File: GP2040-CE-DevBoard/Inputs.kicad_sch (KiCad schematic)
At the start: 21 parts

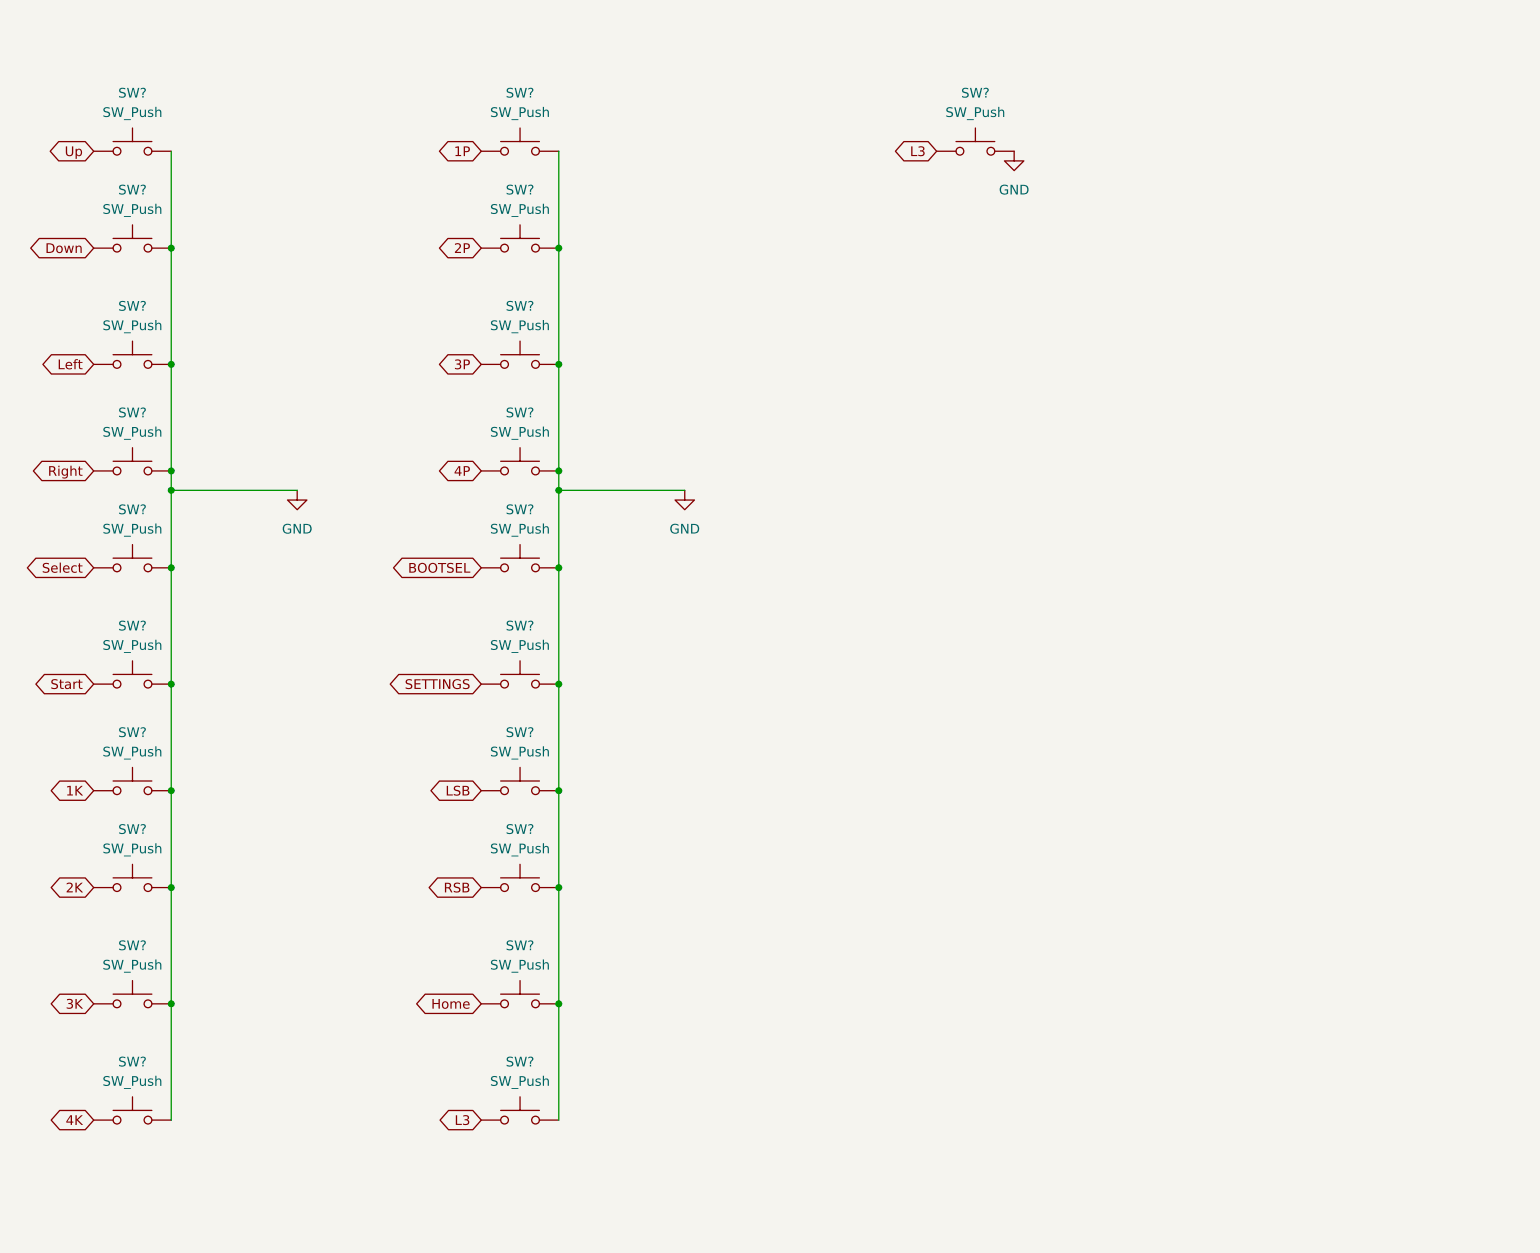
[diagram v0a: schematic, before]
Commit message: Schematic nearly complete, PCB started
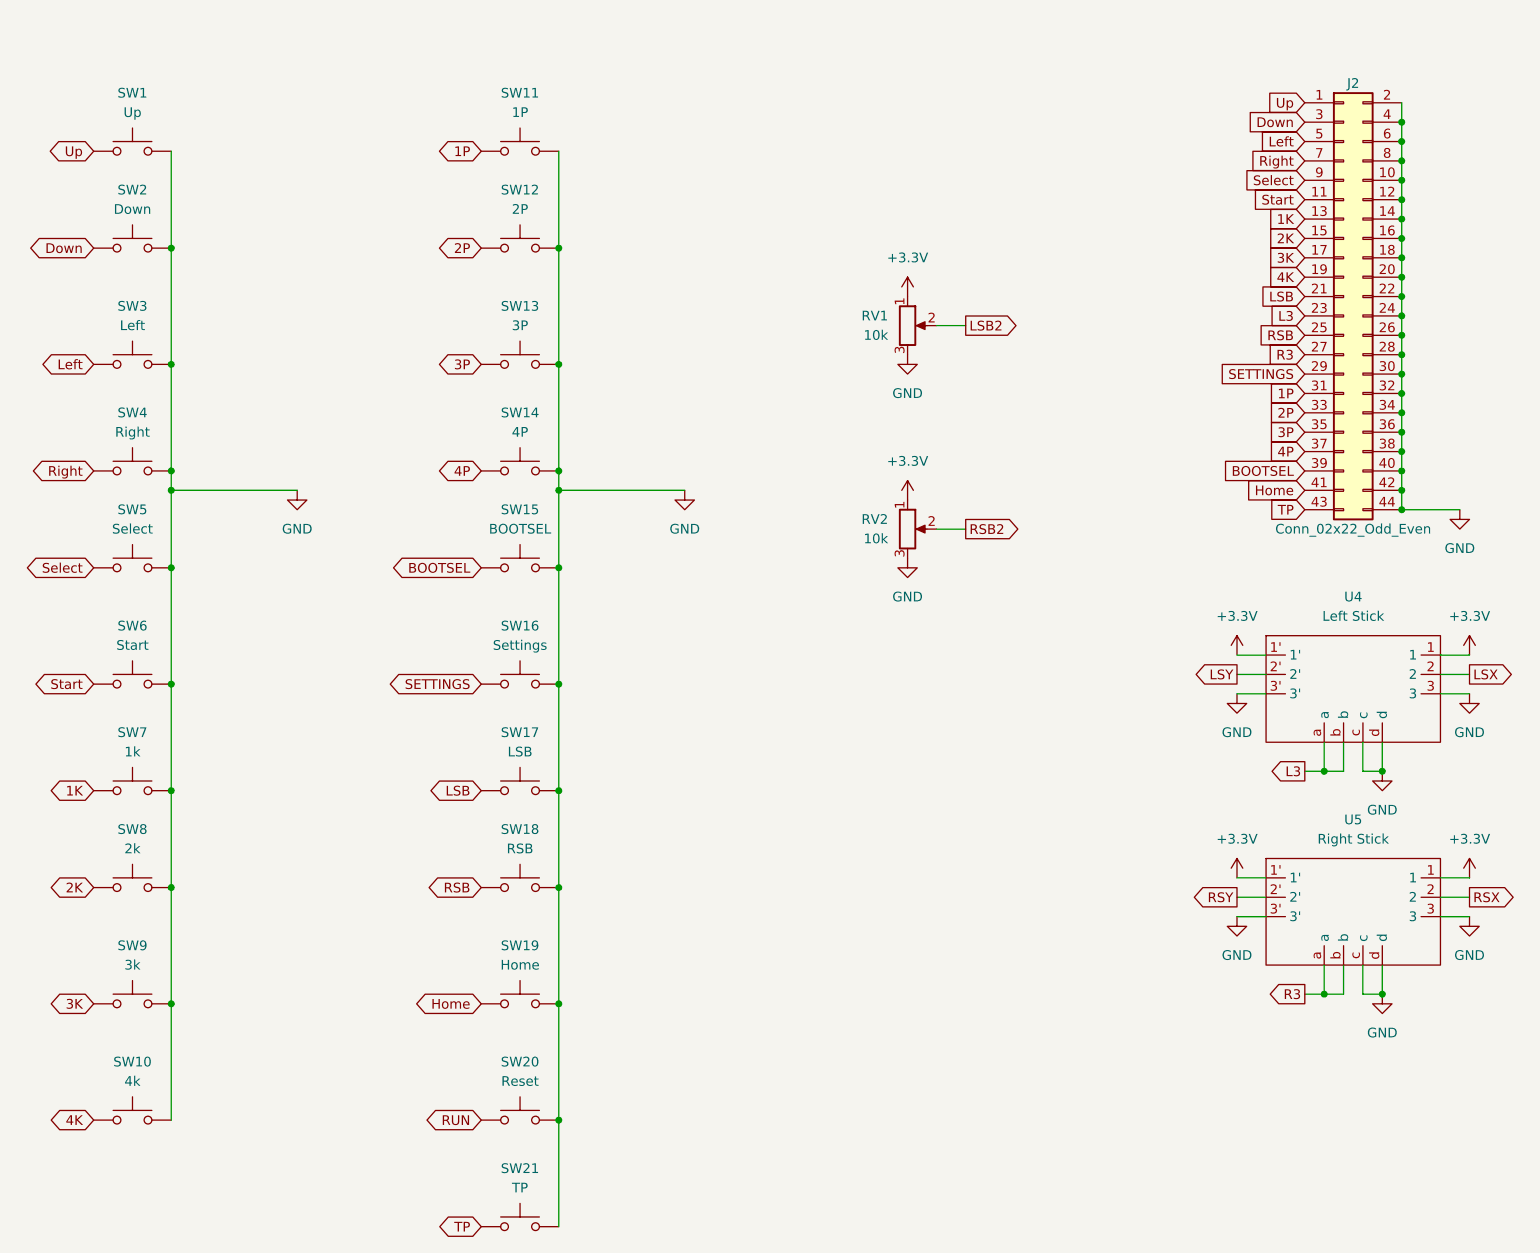
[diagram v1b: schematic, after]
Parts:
- removed SW? (x2): SW_Push, symbol Switch:SW_Push
- added J2: Conn_02x22_Odd_Even, Connector_PinSocket_2.54mm:PinSocket_2x22_P2.54mm_Horizontal, symbol Connector_Generic:Conn_02x22_Odd_Even
- added RV1, RV2: 10k, Potentiometer_THT:Potentiometer_Vishay_148-149_Single_Horizontal, symbol Device:R_Potentiometer
- added SW20: Reset, Button_Switch_SMD:SW_Push_1P1T_NO_6x6mm_H9.5mm, symbol Switch:SW_Push
- added SW21: TP, Button_Switch_SMD:SW_Push_1P1T_NO_6x6mm_H9.5mm, symbol Switch:SW_Push
- added U4: Left Stick, THB001P:THB001P, symbol THB001P:THB001P
- added U5: Right Stick, THB001P:THB001P, symbol THB001P:THB001P
- SW1: renamed from SW?; value SW_Push -> Up; footprint (none) -> Button_Switch_SMD:SW_Push_1P1T_NO_6x6mm_H9.5mm
- SW10: renamed from SW?; value SW_Push -> 4k; footprint (none) -> Button_Switch_SMD:SW_Push_1P1T_NO_6x6mm_H9.5mm
- SW11: renamed from SW?; value SW_Push -> 1P; footprint (none) -> Button_Switch_SMD:SW_Push_1P1T_NO_6x6mm_H9.5mm
- SW12: renamed from SW?; value SW_Push -> 2P; footprint (none) -> Button_Switch_SMD:SW_Push_1P1T_NO_6x6mm_H9.5mm
- SW13: renamed from SW?; value SW_Push -> 3P; footprint (none) -> Button_Switch_SMD:SW_Push_1P1T_NO_6x6mm_H9.5mm
- SW14: renamed from SW?; value SW_Push -> 4P; footprint (none) -> Button_Switch_SMD:SW_Push_1P1T_NO_6x6mm_H9.5mm
- SW15: renamed from SW?; value SW_Push -> BOOTSEL; footprint (none) -> Button_Switch_SMD:SW_Push_1P1T_NO_6x6mm_H9.5mm
- SW16: renamed from SW?; value SW_Push -> Settings; footprint (none) -> Button_Switch_SMD:SW_Push_1P1T_NO_6x6mm_H9.5mm
- SW17: renamed from SW?; value SW_Push -> LSB; footprint (none) -> Button_Switch_SMD:SW_Push_1P1T_NO_6x6mm_H9.5mm
- SW18: renamed from SW?; value SW_Push -> RSB; footprint (none) -> Button_Switch_SMD:SW_Push_1P1T_NO_6x6mm_H9.5mm
- SW19: renamed from SW?; value SW_Push -> Home; footprint (none) -> Button_Switch_SMD:SW_Push_1P1T_NO_6x6mm_H9.5mm
- SW2: renamed from SW?; value SW_Push -> Down; footprint (none) -> Button_Switch_SMD:SW_Push_1P1T_NO_6x6mm_H9.5mm
- SW3: renamed from SW?; value SW_Push -> Left; footprint (none) -> Button_Switch_SMD:SW_Push_1P1T_NO_6x6mm_H9.5mm
- SW4: renamed from SW?; value SW_Push -> Right; footprint (none) -> Button_Switch_SMD:SW_Push_1P1T_NO_6x6mm_H9.5mm
- SW5: renamed from SW?; value SW_Push -> Select; footprint (none) -> Button_Switch_SMD:SW_Push_1P1T_NO_6x6mm_H9.5mm
- SW6: renamed from SW?; value SW_Push -> Start; footprint (none) -> Button_Switch_SMD:SW_Push_1P1T_NO_6x6mm_H9.5mm
- SW7: renamed from SW?; value SW_Push -> 1k; footprint (none) -> Button_Switch_SMD:SW_Push_1P1T_NO_6x6mm_H9.5mm
- SW8: renamed from SW?; value SW_Push -> 2k; footprint (none) -> Button_Switch_SMD:SW_Push_1P1T_NO_6x6mm_H9.5mm
- SW9: renamed from SW?; value SW_Push -> 3k; footprint (none) -> Button_Switch_SMD:SW_Push_1P1T_NO_6x6mm_H9.5mm
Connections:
- net 1K: now also J2.13 (Pin_13)
- net 1P: now also J2.31 (Pin_31)
- net 2K: now also J2.15 (Pin_15)
- net 2P: now also J2.33 (Pin_33)
- net 3K: now also J2.17 (Pin_17)
- net 3P: now also J2.35 (Pin_35)
- net 4K: now also J2.19 (Pin_19)
- net 4P: now also J2.37 (Pin_37)
- net BOOTSEL: now also J2.39 (Pin_39)
- net Down: now also J2.3 (Pin_3)
- net GND: now also J2.10 (Pin_10), J2.12 (Pin_12), J2.14 (Pin_14), J2.16 (Pin_16), J2.18 (Pin_18), J2.2 (Pin_2), J2.20 (Pin_20), J2.22 (Pin_22), J2.24 (Pin_24), J2.26 (Pin_26), J2.28 (Pin_28), J2.30 (Pin_30), J2.32 (Pin_32), J2.34 (Pin_34), J2.36 (Pin_36), J2.38 (Pin_38), J2.4 (Pin_4), J2.40 (Pin_40), J2.42 (Pin_42), J2.44 (Pin_44), J2.6 (Pin_6), J2.8 (Pin_8), RV1.3, RV2.3, SW20.2, SW21.2, U4.3, U4.3', U4.c, U4.d, U5.3, U5.3', U5.c, U5.d
- net Home: now also J2.41 (Pin_41)
- net L3: now also J2.23 (Pin_23), U4.a, U4.b
- net LSB: now also J2.21 (Pin_21)
- net Left: now also J2.5 (Pin_5)
- net RSB: now also J2.25 (Pin_25)
- net Right: now also J2.7 (Pin_7)
- net SETTINGS: now also J2.29 (Pin_29)
- net Select: now also J2.9 (Pin_9)
- net Start: now also J2.11 (Pin_11)
- net Up: now also J2.1 (Pin_1)
- new net +3V3: RV1.1, RV2.1, U4.1, U4.1', U5.1, U5.1'
- new net LSB2: RV1.2
- new net LSX: U4.2
- new net LSY: U4.2'
- new net R3: J2.27 (Pin_27), U5.a, U5.b
- new net RSB2: RV2.2
- new net RSX: U5.2
- new net RSY: U5.2'
- new net RUN: SW20.1
- new net TP: J2.43 (Pin_43), SW21.1

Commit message: Updating schema and PCB design
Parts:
- removed SW17: LSB, Button_Switch_SMD:SW_Push_1P1T_NO_6x6mm_H9.5mm, symbol Switch:SW_Push
- removed SW18: RSB, Button_Switch_SMD:SW_Push_1P1T_NO_6x6mm_H9.5mm, symbol Switch:SW_Push
- J2: symbol Connector_Generic:Conn_02x22_Odd_Even -> Connector_Generic:Conn_02x20_Odd_Even
- SW10: value 4k -> L2
- SW11: value 1P -> B3
- SW12: value 2P -> B4
- SW13: value 3P -> R1
- SW14: value 4P -> L1
- SW17: renamed from SW19; value Home -> A1
- SW19: renamed from SW21; value TP -> A2
- SW5: value Select -> S1
- SW6: value Start -> S2
- SW7: value 1k -> B1
- SW8: value 2k -> B2
- SW9: value 3k -> R2
- renumbered SW20 to SW18
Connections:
- net LSB is gone; now on net L2: J2.21 (Pin_21)
- net BOOTSEL: now also J2.37 (Pin_37); no longer J2.39 (Pin_39)
- net GND: no longer J2.42 (Pin_42), J2.44 (Pin_44)
- net L3: now also J2.29 (Pin_29); no longer J2.23 (Pin_23)
- net R3: now also J2.31 (Pin_31); no longer J2.27 (Pin_27)
- net RUN: now also J2.39 (Pin_39)
- net SETTINGS: no longer J2.29 (Pin_29)
- net 1K renamed B1
- net B1: now also J2.9 (Pin_9); no longer J2.13 (Pin_13)
- net 1P renamed B3
- net B3: now also J2.13 (Pin_13); no longer J2.31 (Pin_31)
- net 2K renamed B2
- net B2: now also J2.11 (Pin_11); no longer J2.15 (Pin_15)
- net 2P renamed A1
- net A1: now also SW17.1; no longer SW12.1
- net 3K renamed L1
- net L1: now also SW14.1; no longer SW9.1
- net 3P renamed A2
- net A2: now also SW19.1; no longer SW13.1
- net 4K renamed L2
- net L2: no longer J2.19 (Pin_19)
- removed net 4P: J2.37 (Pin_37), SW14.1
- removed net Home: J2.41 (Pin_41), SW17.1
- net RSB renamed S1
- net S1: now also SW5.1
- removed net Select: J2.9 (Pin_9), SW5.1
- net Start renamed S2
- net S2: now also J2.27 (Pin_27); no longer J2.11 (Pin_11)
- removed net TP: J2.43 (Pin_43), SW19.1
- new net B4: J2.15 (Pin_15), SW12.1
- new net R1: J2.19 (Pin_19), SW13.1
- new net R2: J2.23 (Pin_23), SW9.1
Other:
- moved on the sheet: SW17, SW18, SW19

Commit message: Progress
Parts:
- removed RV1, RV2: 10k, Potentiometer_THT:Potentiometer_Vishay_148-149_Single_Horizontal, symbol Device:R_Potentiometer
- removed SW1: Up, Button_Switch_SMD:SW_Push_1P1T_NO_6x6mm_H9.5mm, symbol Switch:SW_Push
- removed SW10: L2, Button_Switch_SMD:SW_Push_1P1T_NO_6x6mm_H9.5mm, symbol Switch:SW_Push
- removed SW11: B3, Button_Switch_SMD:SW_Push_1P1T_NO_6x6mm_H9.5mm, symbol Switch:SW_Push
- removed SW12: B4, Button_Switch_SMD:SW_Push_1P1T_NO_6x6mm_H9.5mm, symbol Switch:SW_Push
- removed SW13: R1, Button_Switch_SMD:SW_Push_1P1T_NO_6x6mm_H9.5mm, symbol Switch:SW_Push
- removed SW14: L1, Button_Switch_SMD:SW_Push_1P1T_NO_6x6mm_H9.5mm, symbol Switch:SW_Push
- removed SW15: BOOTSEL, Button_Switch_SMD:SW_Push_1P1T_NO_6x6mm_H9.5mm, symbol Switch:SW_Push
- removed SW16: Settings, Button_Switch_SMD:SW_Push_1P1T_NO_6x6mm_H9.5mm, symbol Switch:SW_Push
- removed SW17: A1, Button_Switch_SMD:SW_Push_1P1T_NO_6x6mm_H9.5mm, symbol Switch:SW_Push
- removed SW18: Reset, Button_Switch_SMD:SW_Push_1P1T_NO_6x6mm_H9.5mm, symbol Switch:SW_Push
- removed SW19: A2, Button_Switch_SMD:SW_Push_1P1T_NO_6x6mm_H9.5mm, symbol Switch:SW_Push
- removed SW2: Down, Button_Switch_SMD:SW_Push_1P1T_NO_6x6mm_H9.5mm, symbol Switch:SW_Push
- removed SW3: Left, Button_Switch_SMD:SW_Push_1P1T_NO_6x6mm_H9.5mm, symbol Switch:SW_Push
- removed SW4: Right, Button_Switch_SMD:SW_Push_1P1T_NO_6x6mm_H9.5mm, symbol Switch:SW_Push
- removed SW5: S1, Button_Switch_SMD:SW_Push_1P1T_NO_6x6mm_H9.5mm, symbol Switch:SW_Push
- removed SW6: S2, Button_Switch_SMD:SW_Push_1P1T_NO_6x6mm_H9.5mm, symbol Switch:SW_Push
- removed SW7: B1, Button_Switch_SMD:SW_Push_1P1T_NO_6x6mm_H9.5mm, symbol Switch:SW_Push
- removed SW8: B2, Button_Switch_SMD:SW_Push_1P1T_NO_6x6mm_H9.5mm, symbol Switch:SW_Push
- removed SW9: R2, Button_Switch_SMD:SW_Push_1P1T_NO_6x6mm_H9.5mm, symbol Switch:SW_Push
- removed U4: Left Stick, THB001P:THB001P, symbol THB001P:THB001P
- removed U5: Right Stick, THB001P:THB001P, symbol THB001P:THB001P
- J2: value Conn_02x22_Odd_Even -> Conn_02x21_Odd_Even; footprint Connector_PinSocket_2.54mm:PinSocket_2x22_P2.54mm_Horizontal -> Connector_PinHeader_2.54mm:PinHeader_2x21_P2.54mm_Vertical; symbol Connector_Generic:Conn_02x20_Odd_Even -> Connector_Generic:Conn_02x21_Odd_Even
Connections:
- net A1: now also J2.34 (Pin_34); no longer J2.33 (Pin_33)
- net A2: now also J2.32 (Pin_32); no longer J2.35 (Pin_35)
- net B1: now also J2.14 (Pin_14); no longer J2.9 (Pin_9)
- net B2: now also J2.16 (Pin_16); no longer J2.11 (Pin_11)
- net B3: now also J2.22 (Pin_22); no longer J2.13 (Pin_13)
- net B4: now also J2.24 (Pin_24); no longer J2.15 (Pin_15)
- net BOOTSEL: now also J2.4 (Pin_4); no longer J2.37 (Pin_37)
- net Down: now also J2.8 (Pin_8); no longer J2.3 (Pin_3)
- net GND: now also J2.1 (Pin_1), J2.11 (Pin_11), J2.13 (Pin_13), J2.15 (Pin_15), J2.17 (Pin_17), J2.19 (Pin_19), J2.21 (Pin_21), J2.23 (Pin_23), J2.25 (Pin_25), J2.27 (Pin_27), J2.29 (Pin_29), J2.3 (Pin_3), J2.31 (Pin_31), J2.33 (Pin_33), J2.35 (Pin_35), J2.37 (Pin_37), J2.39 (Pin_39), J2.41 (Pin_41), J2.5 (Pin_5), J2.7 (Pin_7), J2.9 (Pin_9); no longer J2.10 (Pin_10), J2.12 (Pin_12), J2.14 (Pin_14), J2.16 (Pin_16), J2.18 (Pin_18), J2.2 (Pin_2), J2.20 (Pin_20), J2.22 (Pin_22), J2.24 (Pin_24), J2.26 (Pin_26), J2.28 (Pin_28), J2.30 (Pin_30), J2.32 (Pin_32), J2.34 (Pin_34), J2.36 (Pin_36), J2.38 (Pin_38), J2.4 (Pin_4), J2.40 (Pin_40), J2.6 (Pin_6), J2.8 (Pin_8)
- net L1: now also J2.28 (Pin_28); no longer J2.17 (Pin_17)
- net L2: now also J2.20 (Pin_20); no longer J2.21 (Pin_21)
- net L3: now also J2.38 (Pin_38); no longer J2.29 (Pin_29)
- net Left: now also J2.12 (Pin_12); no longer J2.5 (Pin_5)
- net R1: now also J2.26 (Pin_26); no longer J2.19 (Pin_19)
- net R2: now also J2.18 (Pin_18); no longer J2.23 (Pin_23)
- net R3: now also J2.36 (Pin_36); no longer J2.31 (Pin_31)
- net RUN: now also J2.30 (Pin_30); no longer J2.39 (Pin_39)
- net Right: now also J2.10 (Pin_10); no longer J2.7 (Pin_7)
- net S1: now also J2.42 (Pin_42); no longer J2.25 (Pin_25)
- net S2: now also J2.40 (Pin_40); no longer J2.27 (Pin_27)
- net SETTINGS: now also J2.2 (Pin_2)
- net Up: now also J2.6 (Pin_6); no longer J2.1 (Pin_1)

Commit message: a lot of Silkscreen work
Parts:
- added J2, J4: Conn_01x04, Connector_PinHeader_2.54mm:PinHeader_1x05_P2.54mm_Vertical, symbol Connector_Generic:Conn_01x05
- added J3: Conn_01x03, symbol Connector_Generic:Conn_01x03
- added J5: Conn_01x03, Connector_PinHeader_2.54mm:PinHeader_1x03_P2.54mm_Vertical, symbol Connector_Generic:Conn_01x03
- renumbered J2 to J6
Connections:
- net GND: now also J2.5 (Pin_5), J3.3 (Pin_3), J4.5 (Pin_5), J5.3 (Pin_3)
- net L3: now also J4.4 (Pin_4)
- net R3: now also J2.4 (Pin_4)
- new net +3V3: J2.1 (Pin_1), J3.1 (Pin_1), J4.1 (Pin_1), J5.1 (Pin_1)
- new net LSB2: J5.2 (Pin_2)
- new net LSX: J4.2 (Pin_2)
- new net LSY: J4.3 (Pin_3)
- new net RSB2: J3.2 (Pin_2)
- new net RSX: J2.2 (Pin_2)
- new net RSY: J2.3 (Pin_3)
